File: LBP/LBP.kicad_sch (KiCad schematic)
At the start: 28 parts, among them U1 OPA1641, U2 OPA1641, U3 OPA1641, U4 OPA1641

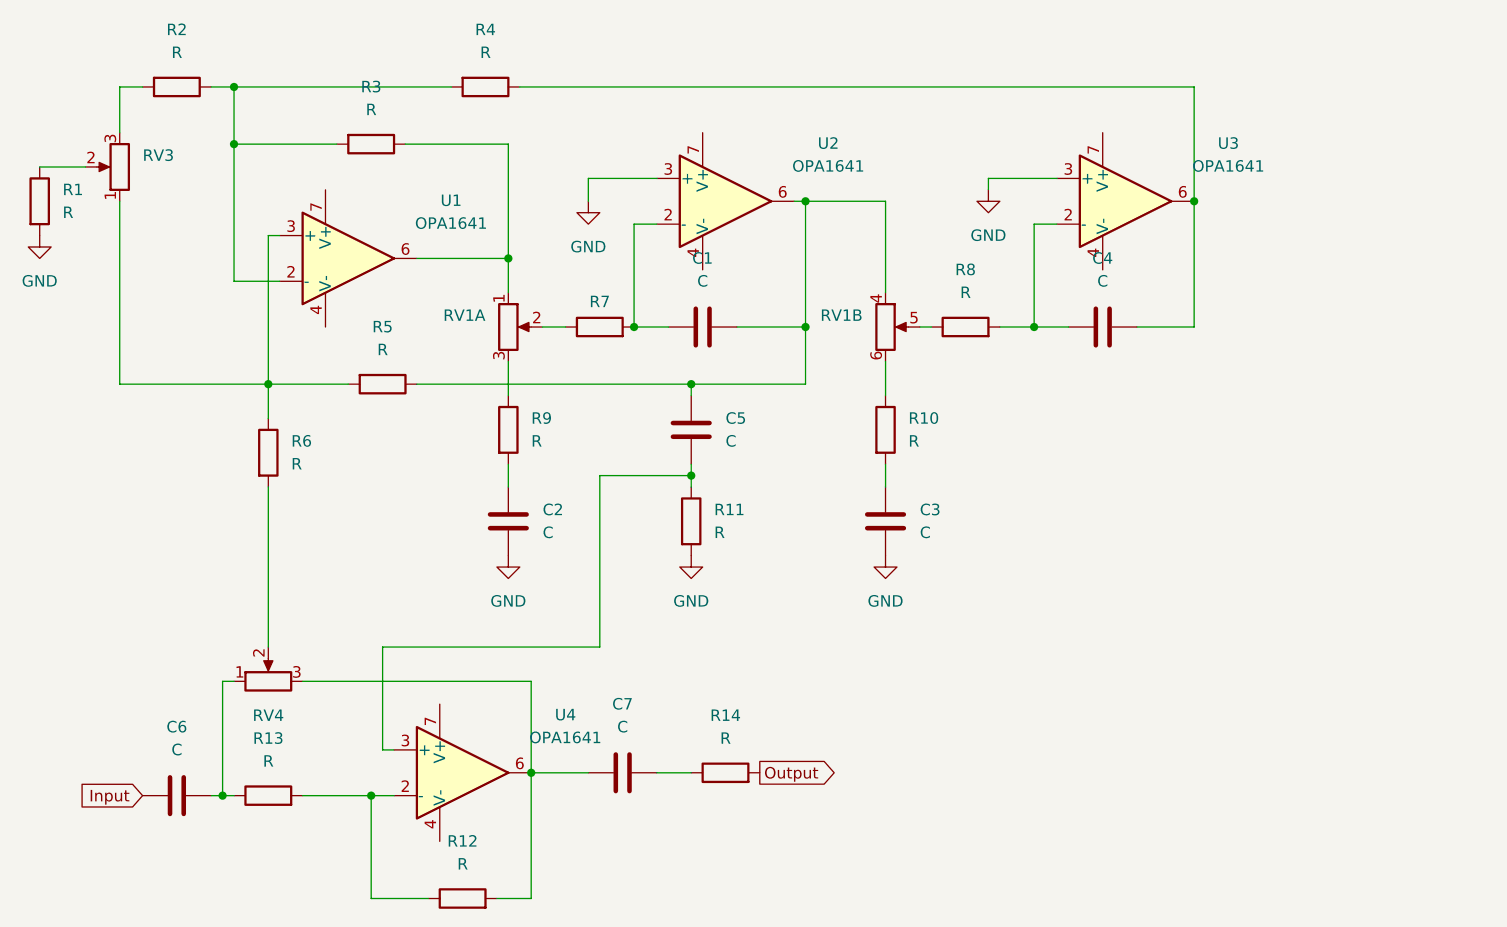
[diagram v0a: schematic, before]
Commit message: New Voltage lines
Added +15 and -15 Voltage rails to Op-Amps
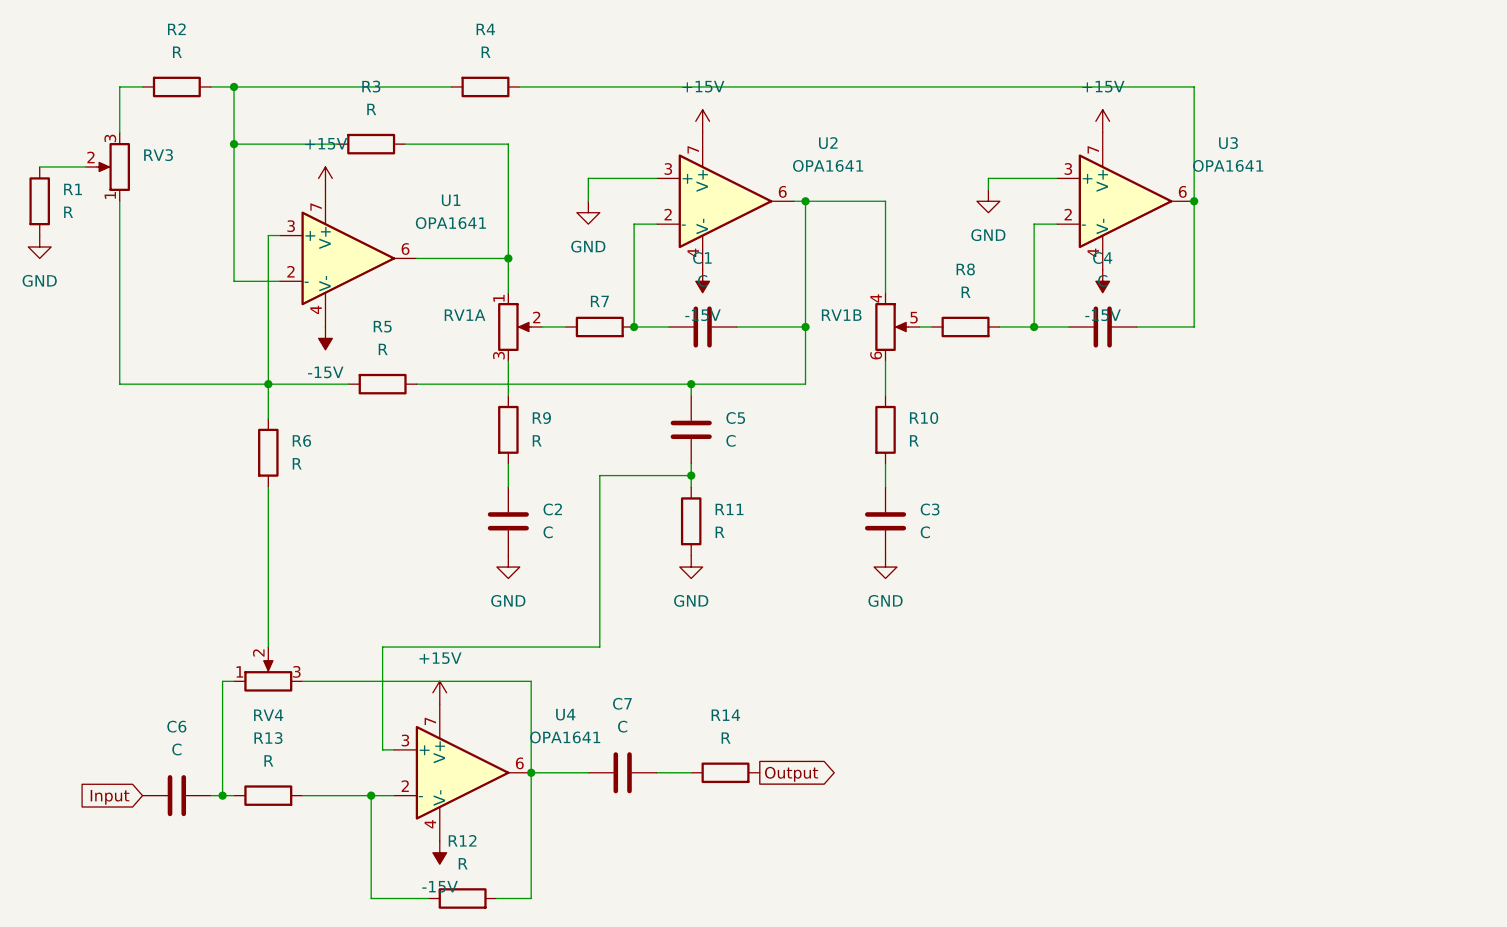
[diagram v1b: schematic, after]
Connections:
- net -15V: now reaches U3.4 (V-)
- net -15V: now also U1.4 (V-), U2.4 (V-), U4.4 (V-)
- net +15V: now reaches U3.7 (V+)
- net +15V: now also U1.7 (V+), U2.7 (V+), U4.7 (V+)

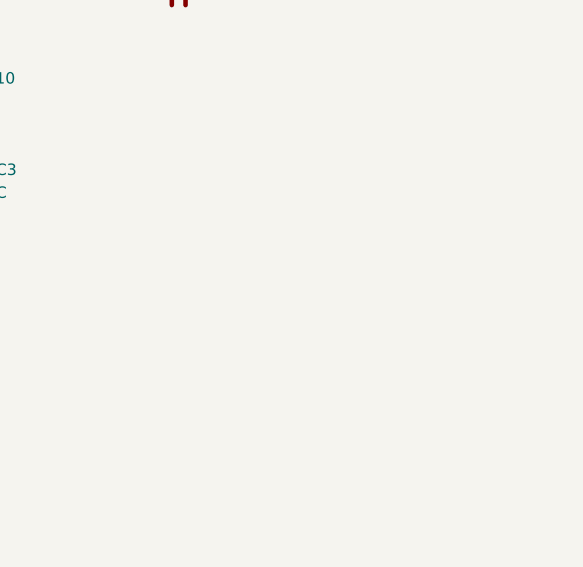
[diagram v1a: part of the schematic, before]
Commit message: added temp opamp
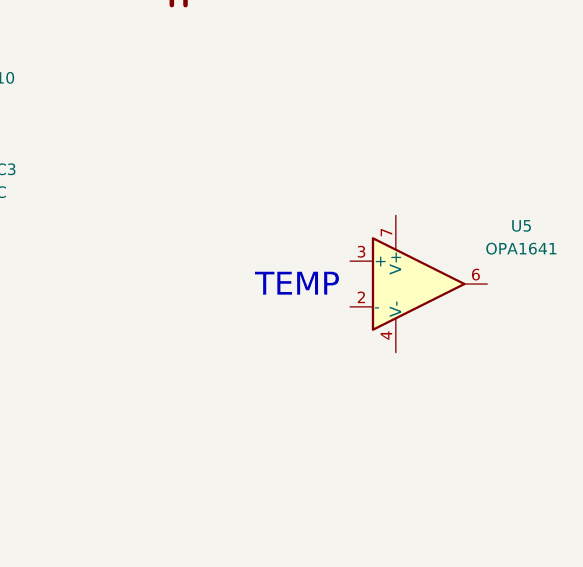
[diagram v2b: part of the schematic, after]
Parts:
- added U5: OPA1641, symbol Amplifier_Operational:OPA1641
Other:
- note added: "TEMP"
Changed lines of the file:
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@@
 		(rev "1.0")
+	)
+	(text "TEMP"
+		(exclude_from_sim no)
+		(at 151.638 81.534 0)
+		(effects
+			(font
+				(size 2.54 2.54)
+			)
+		)
 	)
 	(junction
@@
 					(unit 1)
 				)
+			)
+		)
+	)
+	(symbol
+		(lib_id "Amplifier_Operational:OPA1641")
+		(at 165.1 81.28 0)
+		(unit 1)
+		(exclude_from_sim no)
+		(in_bom yes)
+		(on_board yes)
+		(dnp no)
+		(fields_autoplaced yes)
+		(property "Reference" "U5"
+			(at 176.53 74.8598 0)
+			(effects
+				(font
+					(size 1.27 1.27)
+				)
+			)
+		)
+		(property "Value" "OPA1641"
+			(at 176.53 77.3998 0)
+			(effects
+				(font
+					(size 1.27 1.27)
+				)
+			)
+		)
+		(property "Footprint" ""
+			(at 165.1 81.28 0)
+			(effects
+				(font
+					(size 1.27 1.27)
+				)
+				(hide yes)
+			)
+		)
+		(property "Datasheet" "http://www.ti.com/lit/ds/symlink/opa1641.pdf"
+			(at 165.1 81.28 0)
+			(effects
+				(font
+					(size 1.27 1.27)
+				)
+				(hide yes)
+			)
+		)
+		(property "Description" "JFET input, ultralow distortion, low-noise operational amplifier, SOIC-8/VSSOP-8"
+			(at 165.1 81.28 0)
+			(effects
+				(font
+					(size 1.27 1.27)
+				)
+				(hide yes)
+			)
+		)
+		(pin "2"
+		)
+		(pin "3"
+		)
+		(pin "7"
+		)
+		(pin "1"
+		)
+		(pin "5"
+		)
+		(pin "8"
+		)
+		(pin "4"
+		)
+		(pin "6"
+		)
+		(instances
+			(project "LBP"
+				(path "/e9c605b8-0261-4625-b036-2a547cf6d32d"
+					(reference "U5")
+					(unit 1)
+				)

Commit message: LTspice jazz
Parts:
- removed U5: OPA1641, symbol Amplifier_Operational:OPA1641
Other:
- note removed: "TEMP"
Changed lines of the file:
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@@
 		(rev "1.0")
-	)
-	(text "TEMP"
-		(exclude_from_sim no)
-		(at 151.638 81.534 0)
-		(effects
-			(font
-				(size 2.54 2.54)
-			)
-		)
 	)
 	(junction
@@
 					(unit 1)
 				)
-			)
-		)
-	)
-	(symbol
-		(lib_id "Amplifier_Operational:OPA1641")
-		(at 165.1 81.28 0)
-		(unit 1)
-		(exclude_from_sim no)
-		(in_bom yes)
-		(on_board yes)
-		(dnp no)
-		(fields_autoplaced yes)
-		(property "Reference" "U5"
-			(at 176.53 74.8598 0)
-			(effects
-				(font
-					(size 1.27 1.27)
-				)
-			)
-		)
-		(property "Value" "OPA1641"
-			(at 176.53 77.3998 0)
-			(effects
-				(font
-					(size 1.27 1.27)
-				)
-			)
-		)
-		(property "Footprint" ""
-			(at 165.1 81.28 0)
-			(effects
-				(font
-					(size 1.27 1.27)
-				)
-				(hide yes)
-			)
-		)
-		(property "Datasheet" "http://www.ti.com/lit/ds/symlink/opa1641.pdf"
-			(at 165.1 81.28 0)
-			(effects
-				(font
-					(size 1.27 1.27)
-				)
-				(hide yes)
-			)
-		)
-		(property "Description" "JFET input, ultralow distortion, low-noise operational amplifier, SOIC-8/VSSOP-8"
-			(at 165.1 81.28 0)
-			(effects
-				(font
-					(size 1.27 1.27)
-				)
-				(hide yes)
-			)
-		)
-		(pin "2"
-		)
-		(pin "3"
-		)
-		(pin "7"
-		)
-		(pin "1"
-		)
-		(pin "5"
-		)
-		(pin "8"
-		)
-		(pin "4"
-		)
-		(pin "6"
-		)
-		(instances
-			(project "LBP"
-				(path "/e9c605b8-0261-4625-b036-2a547cf6d32d"
-					(reference "U5")
-					(unit 1)
-				)
